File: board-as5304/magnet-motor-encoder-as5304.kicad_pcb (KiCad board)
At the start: 2 copper layers, 38.4 x 11.8 mm, 12 parts, among them U1 DS18B20, U2 AS5304(A)

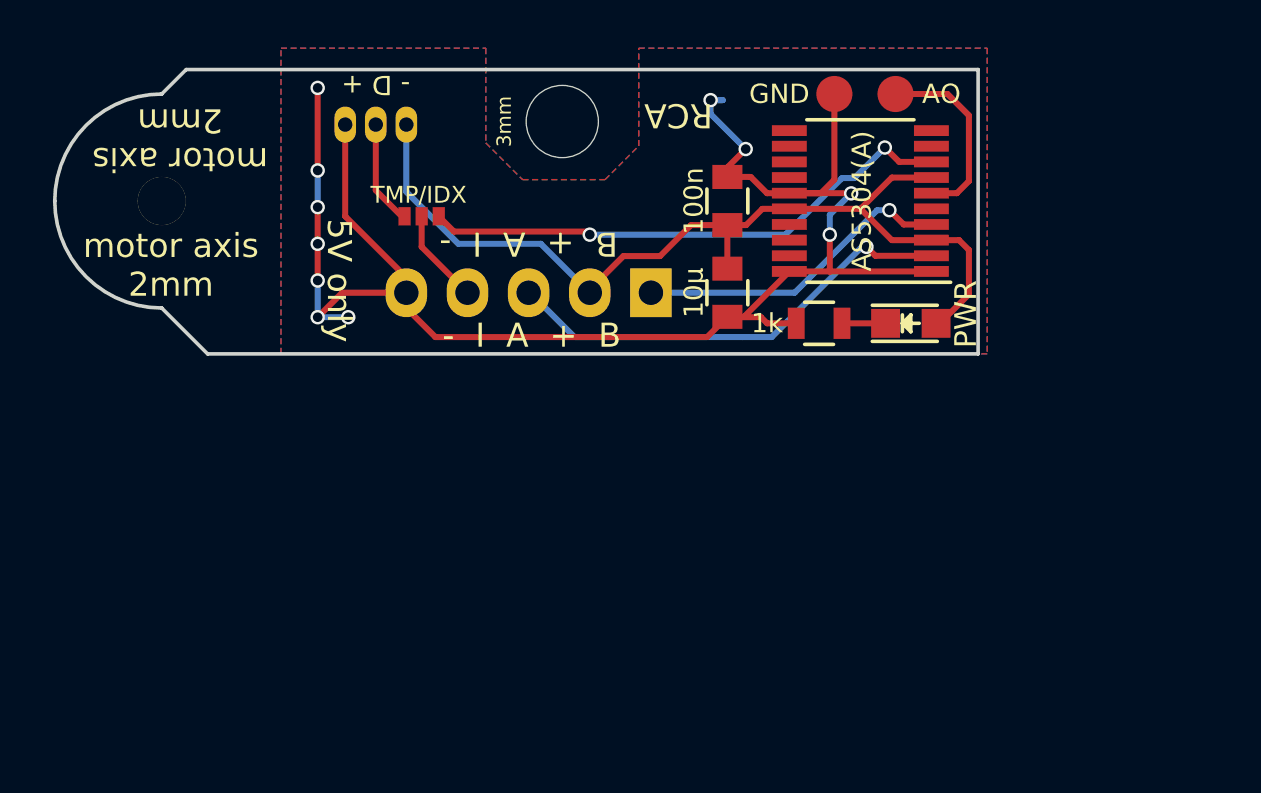
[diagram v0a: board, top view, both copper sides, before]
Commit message: board as5304: rearrange components
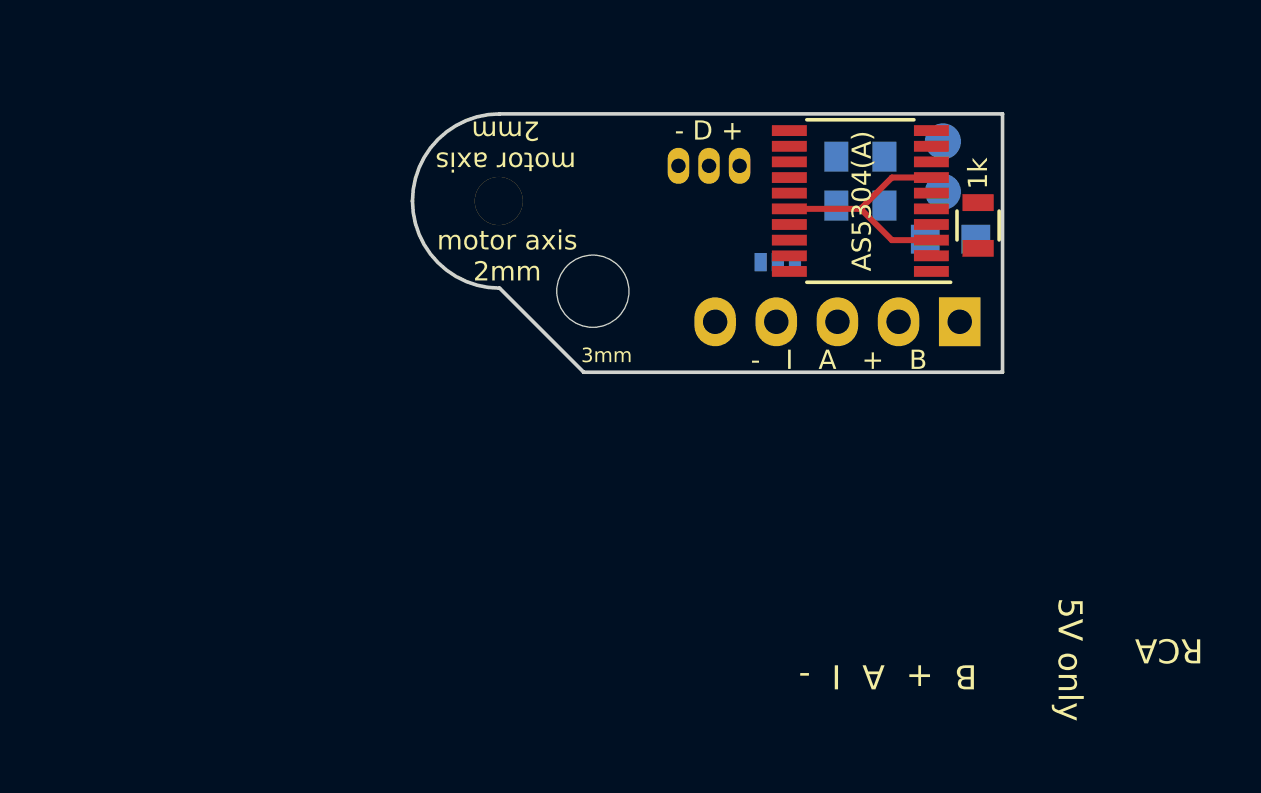
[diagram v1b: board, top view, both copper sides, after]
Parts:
- C1, C2, D1, SJ1, W1, W2: moved to B.Cu
- moved SJ1 14.9 mm to (99.3, 49.5)
- moved REF** 14.0 mm to (87.7, 47.0)
- moved U1 13.9 mm to (95.1, 45.5)
- moved JP1 12.9 mm to (106.8, 52.0)
- moved R1 7.75 mm to (107.6, 48.0), turned to 90 degrees
- moved REF** 7.16 mm to (91.6, 50.7)
- moved C2 6.60 mm to (102.7, 47.2), turned to 0 degrees
- moved C1 5.82 mm to (102.7, 45.1), turned to 0 degrees
- moved W1 4.92 mm to (106.1, 44.5)
- moved W2 4.52 mm to (106.1, 46.6), turned to 180 degrees
- moved D1 3.86 mm to (106.4, 48.6), turned to 180 degrees
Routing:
- net GND: track 69.8 -> 0.00 mm, vias 11 -> 0
- net +5V: track 39.1 -> 9.92 mm
- net /IDX: track 22.5 -> 0.00 mm, vias 2 -> 0
- net /A: track 19.2 -> 0.00 mm, vias 1 -> 0
- net /B: track 13.3 -> 0.00 mm, vias 1 -> 0
- net /AO: track 7.91 -> 0.00 mm
- net /TMP: track 4.37 -> 0.00 mm
- net /TMP_IDX: track 3.96 -> 0.00 mm
- net Net-(D1-Pad1): track 1.81 -> 0.00 mm
- removed copper zone on B.Cu, net GND
- removed copper zone on F.Cu, net GND
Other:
- board size 38.4 x 11.8 mm -> 24.5 x 10.7 mm

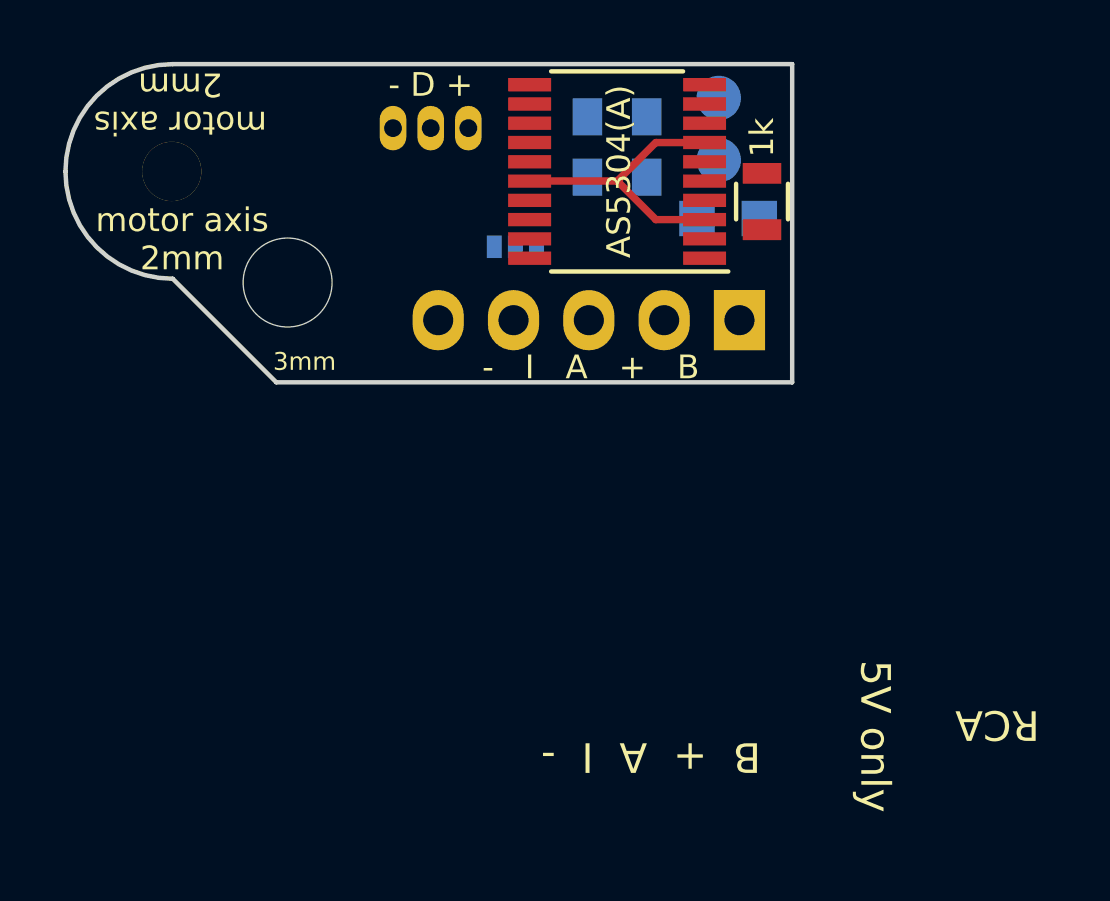
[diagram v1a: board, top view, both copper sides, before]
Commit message: board as5304: finish pcb layout and silkscreen for rev_02
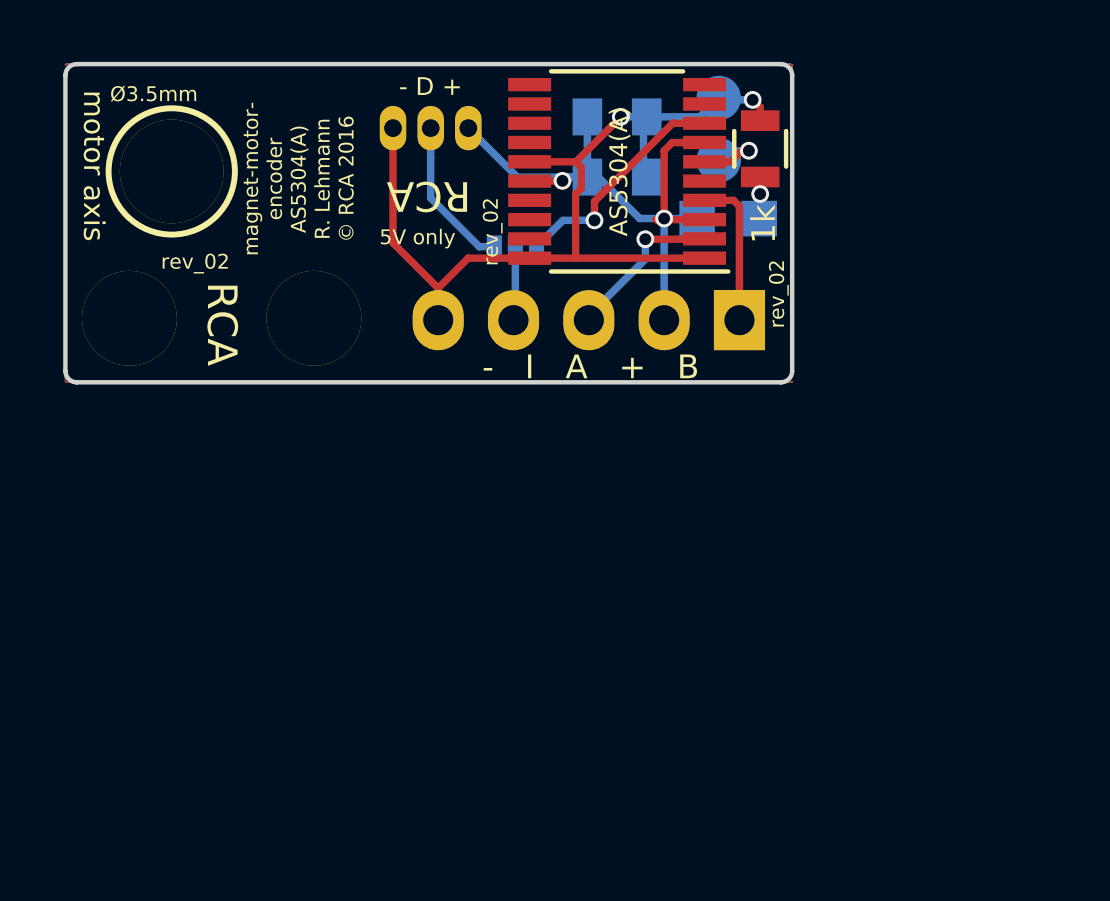
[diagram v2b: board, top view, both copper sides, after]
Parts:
- removed REF**: 3mm, Mounting_Holes:MountingHole_3mm
- removed REF**: Axis 2mm, bjh-kicad-mountingholes-fp:MountingHole_2-0mm
- added REF1: motor axis, MoutingHolesFine:MountingHole_3-5mm, F.Cu at (87.7, 47.0)
- added REF2: mnt. hole, MoutingHolesFine:MountingHole_3-2mm, F.Cu at (92.5, 51.9)
- added REF2: mnt. hole, MoutingHolesFine:MountingHole_3-2mm, F.Cu at (86.2, 51.9)
- moved R1 1.78 mm to (107.5, 46.2)
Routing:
- net GND: track 0.00 -> 31.3 mm, vias 0 -> 2
- net +5V: track 9.92 -> 22.1 mm, vias 0 -> 2
- net /IDX: track 0.00 -> 7.77 mm, vias 0 -> 1
- net /A: track 0.00 -> 5.52 mm, vias 0 -> 1
- net /TMP: track 0.00 -> 5.18 mm
- net /B: track 0.00 -> 5.10 mm
- net /AO: track 0.00 -> 2.80 mm, vias 0 -> 1
- net /TMP_IDX: track 0.00 -> 2.66 mm
- net Net-(D1-Pad1): track 0.00 -> 1.41 mm, vias 0 -> 1
- added copper zone on B.Cu, net GND
- added copper zone on F.Cu, net GND
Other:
- outline, holes or cut-outs redrawn
- rule pad_to_mask_clearance: 0.2 -> 0.1
- board text added: "magnet-motor- encoder AS5304(A) R. Lehmann © RCA 2016"
- board text added: "motor axis"
- board text added: "rev_02"
- board text added: "Ø3.5mm"
- board text removed: "magnet-motor- encoder AS5304(A) A. Wenzel R. Lehmann © RCA 2016"
- board text removed: "motor axis 2mm"

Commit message: board as5304: replace most 0805 Rs and Cs with 0603 packages
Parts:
- C1: footprint Capacitors_SMD:C_0805 -> Capacitors_SMD:C_0603
- D1: footprint LEDs:LED_0805 -> LEDs:LED_0603
- R1: footprint Resistors_SMD:R_0805 -> Resistors_SMD:R_0603
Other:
- board text added: "rev_03"
- board text removed: "rev_02"

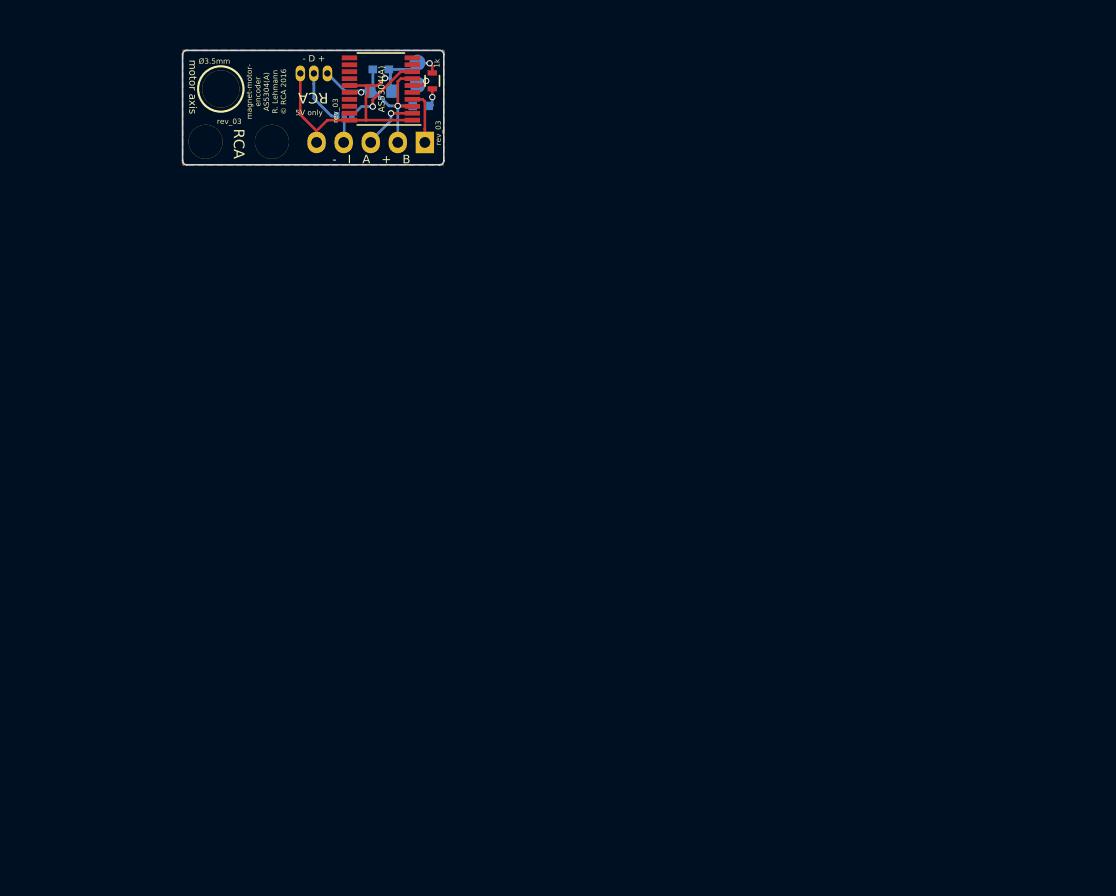
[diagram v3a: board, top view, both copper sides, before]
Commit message: board as5304: new board shape (imported from 3d-model/solidworks); rev_04 tag
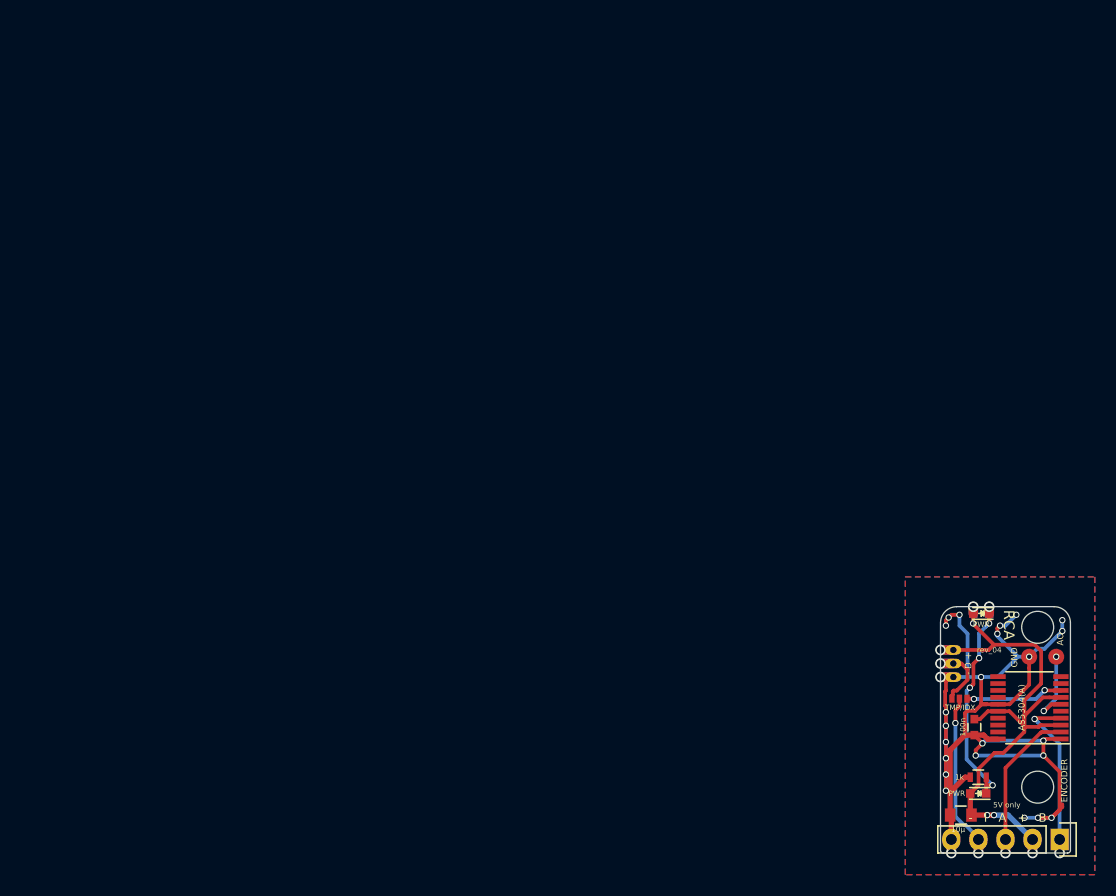
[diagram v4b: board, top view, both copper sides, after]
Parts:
- removed REF1: motor axis, MoutingHolesFine:MountingHole_3-5mm
- removed REF2 (x2): mnt. hole, MoutingHolesFine:MountingHole_3-2mm
- added D2: PWR, LEDs:LED_0603, B.Cu at (159.0, 96.2)
- added D2: PWR, LEDs:LED_0603, F.Cu at (159.0, 96.2)
- C1, C2, D1, JP1, SJ1, W1, W2: moved to F.Cu
- moved JP1 88.5 mm to (166.4, 117.4), turned to 270 degrees
- moved C2 87.1 mm to (157.1, 115.1), turned to 180 degrees
- moved U2 84.1 mm to (163.5, 105.1)
- moved U1 83.4 mm to (156.4, 102.2), turned to 90 degrees
- moved C1 83.1 mm to (158.4, 106.9), turned to 270 degrees
- moved D1 83.1 mm to (158.7, 113.1)
- moved R1 83.0 mm to (158.7, 111.6), turned to 180 degrees
- moved W2 80.5 mm to (166.1, 100.3)
- moved W1 80.0 mm to (163.5, 100.3)
- moved SJ1 79.5 mm to (157.0, 104.2)
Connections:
- net Net-(D1-Pad1) renamed /LED
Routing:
- net GND: track 30.8 -> 112.0 mm, vias 2 -> 25
- net +5V: track 22.1 -> 59.3 mm, vias 2 -> 6
- net /LED: track 1.41 -> 24.0 mm, vias 1 -> 5
- net /TMP_IDX: track 2.66 -> 16.9 mm, vias 0 -> 2
- net /B: track 5.10 -> 17.3 mm, vias 0 -> 2
- net /A: track 5.52 -> 15.9 mm
- net /AO: track 2.85 -> 7.44 mm, vias 1 -> 2
- net /TMP: track 5.18 -> 7.50 mm, vias 0 -> 1
- net /IDX: track 7.77 -> 9.18 mm, vias 1 -> 2
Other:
- board size 24.5 x 10.7 mm -> 12.2 x 23.1 mm
- board text added: "rev_04"
- board text removed: "motor axis"
- board text removed: "rev_03"
- board text removed: "Ø3.5mm"
